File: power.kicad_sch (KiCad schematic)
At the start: 32 parts, among them J3 Screw_Terminal_01x02, SW1 SW_DIP_x01, SW2 SW_DIP_x01, U14 LM2940S-5.0/NOPB

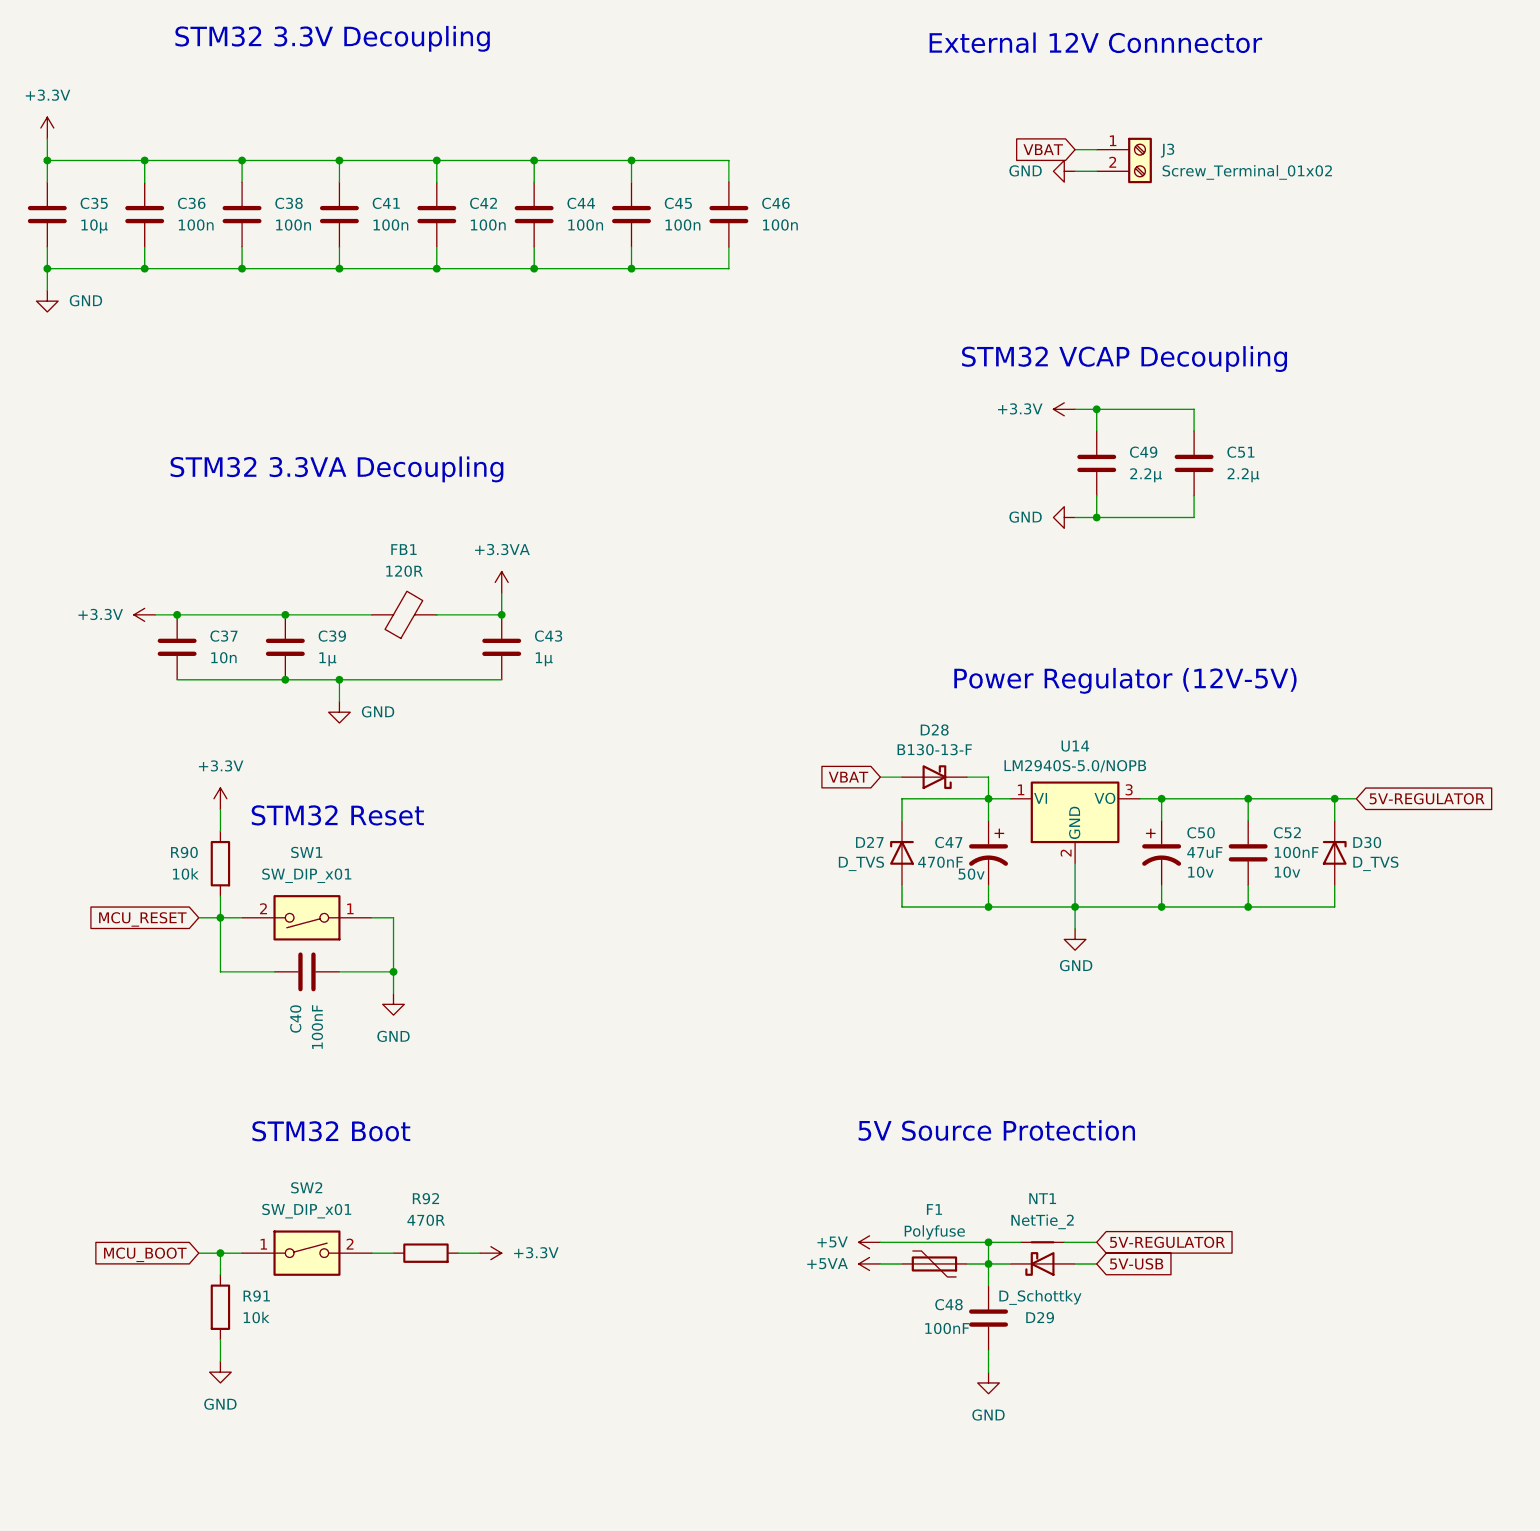
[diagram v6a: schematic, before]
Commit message: Change power layout, add low frequency crystal
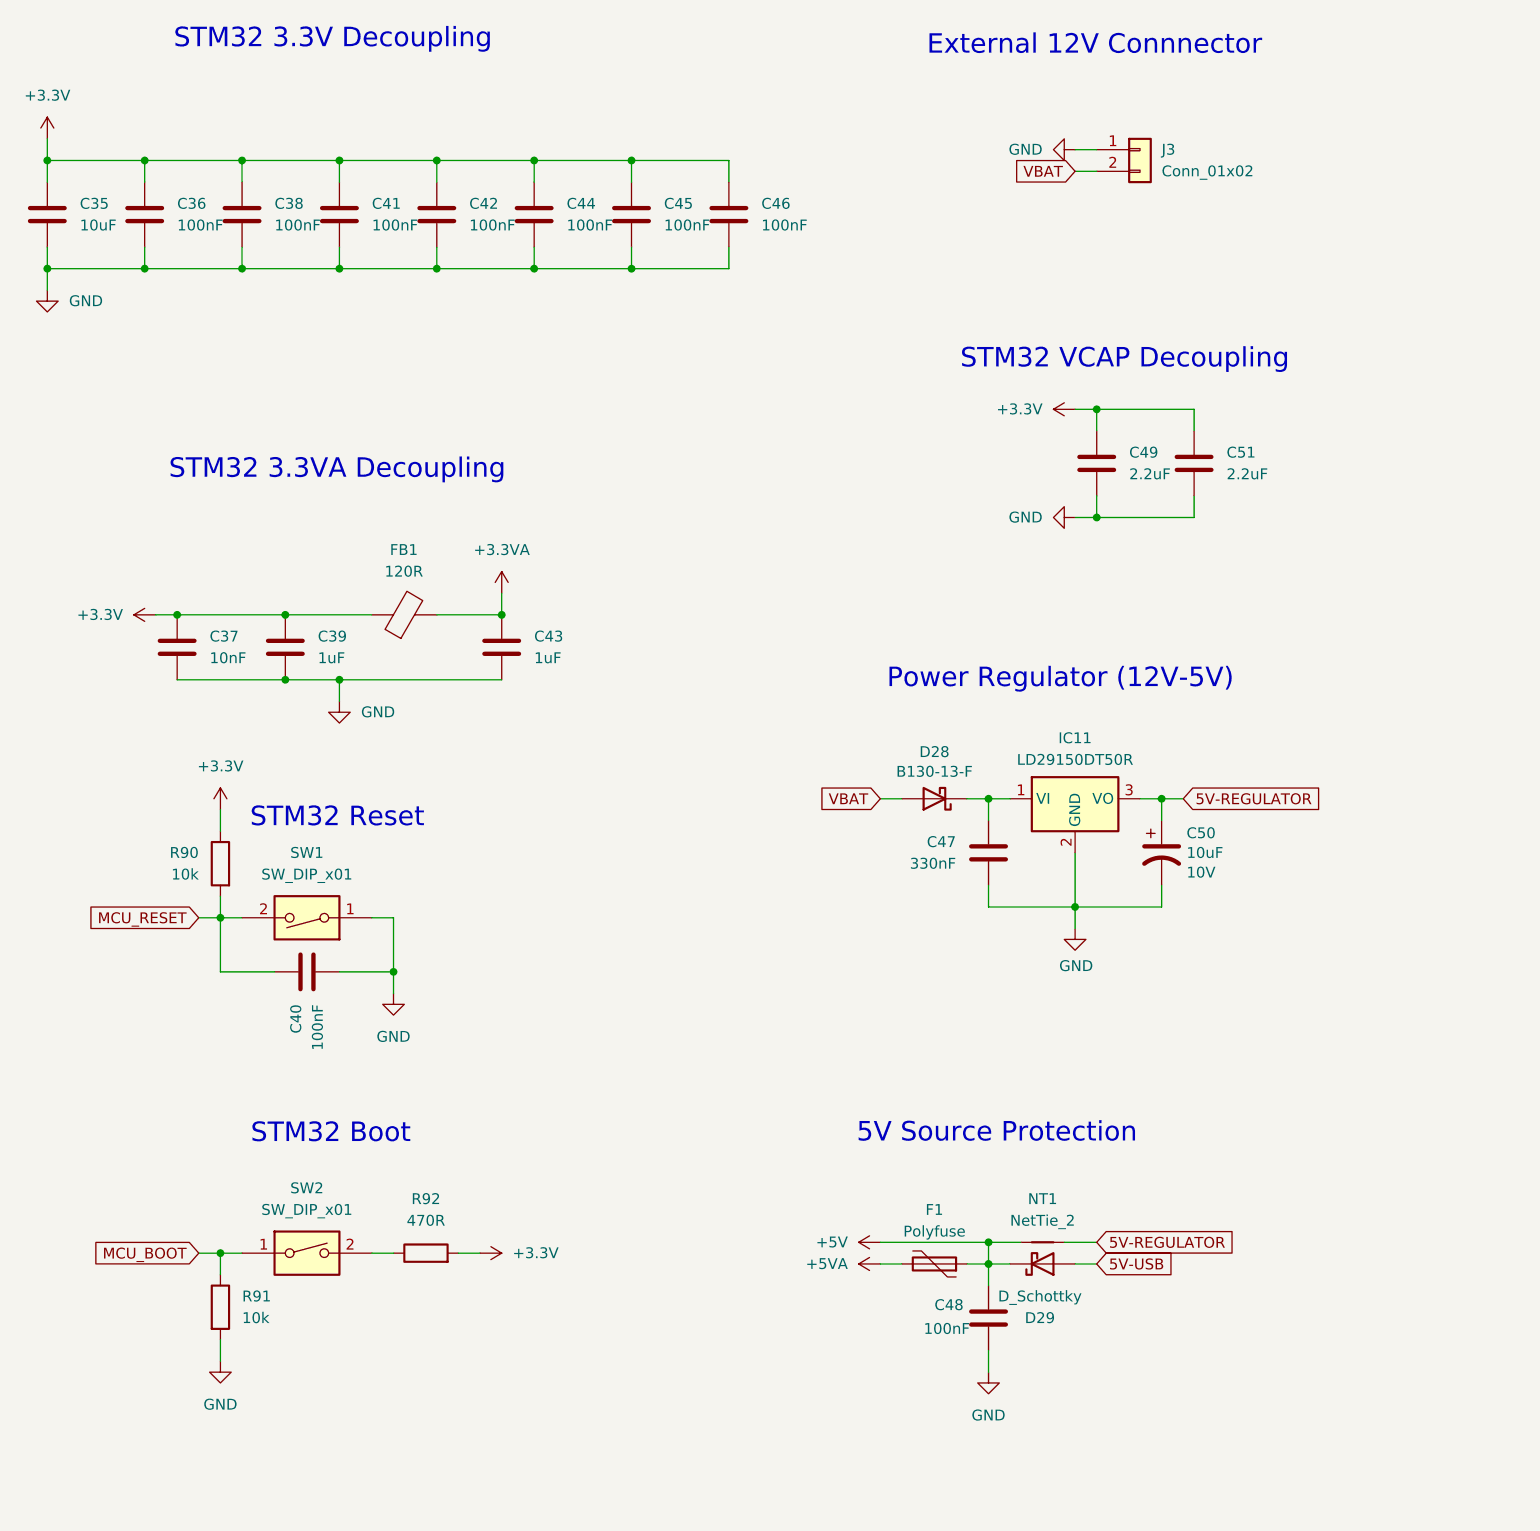
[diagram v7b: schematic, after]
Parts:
- removed C47: 470nF, Capacitor_Tantalum_SMD:CP_EIA-7343-31_Kemet-D, symbol Device:CP1
- removed C52: 100nF, Capacitor_SMD:C_0805_2012Metric, symbol Device:C
- removed D27, D30: D_TVS, Diode_SMD:D_SMB, symbol Device:D_Zener
- removed J3: Screw_Terminal_01x02, TerminalBlock_MetzConnect:TerminalBlock_MetzConnect_Type059_RT06302HBWC_1x02_P3.50mm_Horizontal, symbol Connector:Screw_Terminal_01x02
- removed U14: LM2940S-5.0/NOPB, IC_Automotive:TO-263-3_TabPin2-Clean, symbol Regulator_Linear:LM2937xS
- added C47: 330nF, Capacitor_SMD:C_0805_2012Metric, symbol Device:C
- added IC11: LD29150DT50R, Package_TO_SOT_SMD:TO-252-2, symbol Misc:LD29150DT50R
- added J3: Conn_01x02, Connector_AMASS:AMASS_XT30U-F_1x02_P5.0mm_Vertical, symbol Connector_Generic:Conn_01x02
- C35: value 10µ -> 10uF
- C36, C38, C41, C42, C44, C45, C46: value 100n -> 100nF
- C37: value 10n -> 10nF
- C39, C43: value 1µ -> 1uF
- C49, C51: value 2.2µ -> 2.2uF
- C50: value 47uF -> 10uF; footprint Capacitor_Tantalum_SMD:CP_EIA-3528-21_Kemet-B -> Capacitor_Tantalum_SMD:CP_EIA-3528-12_Kemet-T; Voltage 10v -> 10V
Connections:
- net 5V-REGULATOR: now also IC11.3 (VO)
- net GND: now also C47.2, IC11.2 (GND), J3.1 (Pin_1)
- net VBAT: now also J3.2 (Pin_2)
- net at D28.1 (K): now also C47.1, IC11.1 (VI)
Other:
- moved on the sheet: D28
